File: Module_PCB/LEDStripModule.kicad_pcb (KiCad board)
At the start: 2 copper layers, 247.5 x 25 mm, 107 parts, among them J2 ISP, J4 DS, J5 US, Q1 KIA50N03B, Q2 KIA50N03B, Q3 KIA50N03B, Q4 KIA50N03B, U1 W25Q16JV, U2 AP1117-33, U3 TPS563200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

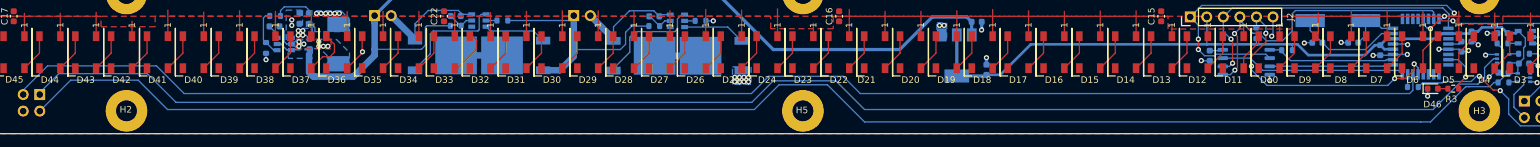
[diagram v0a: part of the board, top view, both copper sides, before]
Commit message: Added test pads
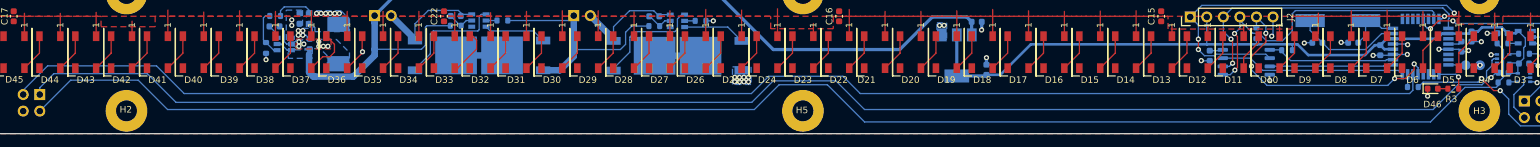
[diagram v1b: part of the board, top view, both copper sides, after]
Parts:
- added TP1: TP, TestPoint:TestPoint_Pad_D1.5mm, B.Cu at (245.4, 114.5)
- added TP2: GND, TestPoint:TestPoint_Pad_D1.5mm, B.Cu at (247.6, 114.5)
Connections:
- U5 pad 23: /LED -> Net-(U5-Pad23)
- U5 pad 24: Net-(U5-Pad24) -> /TP1
- U5 pad 25: Net-(U5-Pad25) -> /LED
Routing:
- net /TP1: track 0.00 -> 2.67 mm
- net /LED: track 6.87 -> 4.98 mm
- net /TRIGI: track 234.1 -> 235.0 mm
- net GND: track 37.1 -> 36.3 mm, vias 38 -> 39
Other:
- board text added: "GND"
- board text added: "TP1"
